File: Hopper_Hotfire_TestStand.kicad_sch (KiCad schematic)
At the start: 28 parts

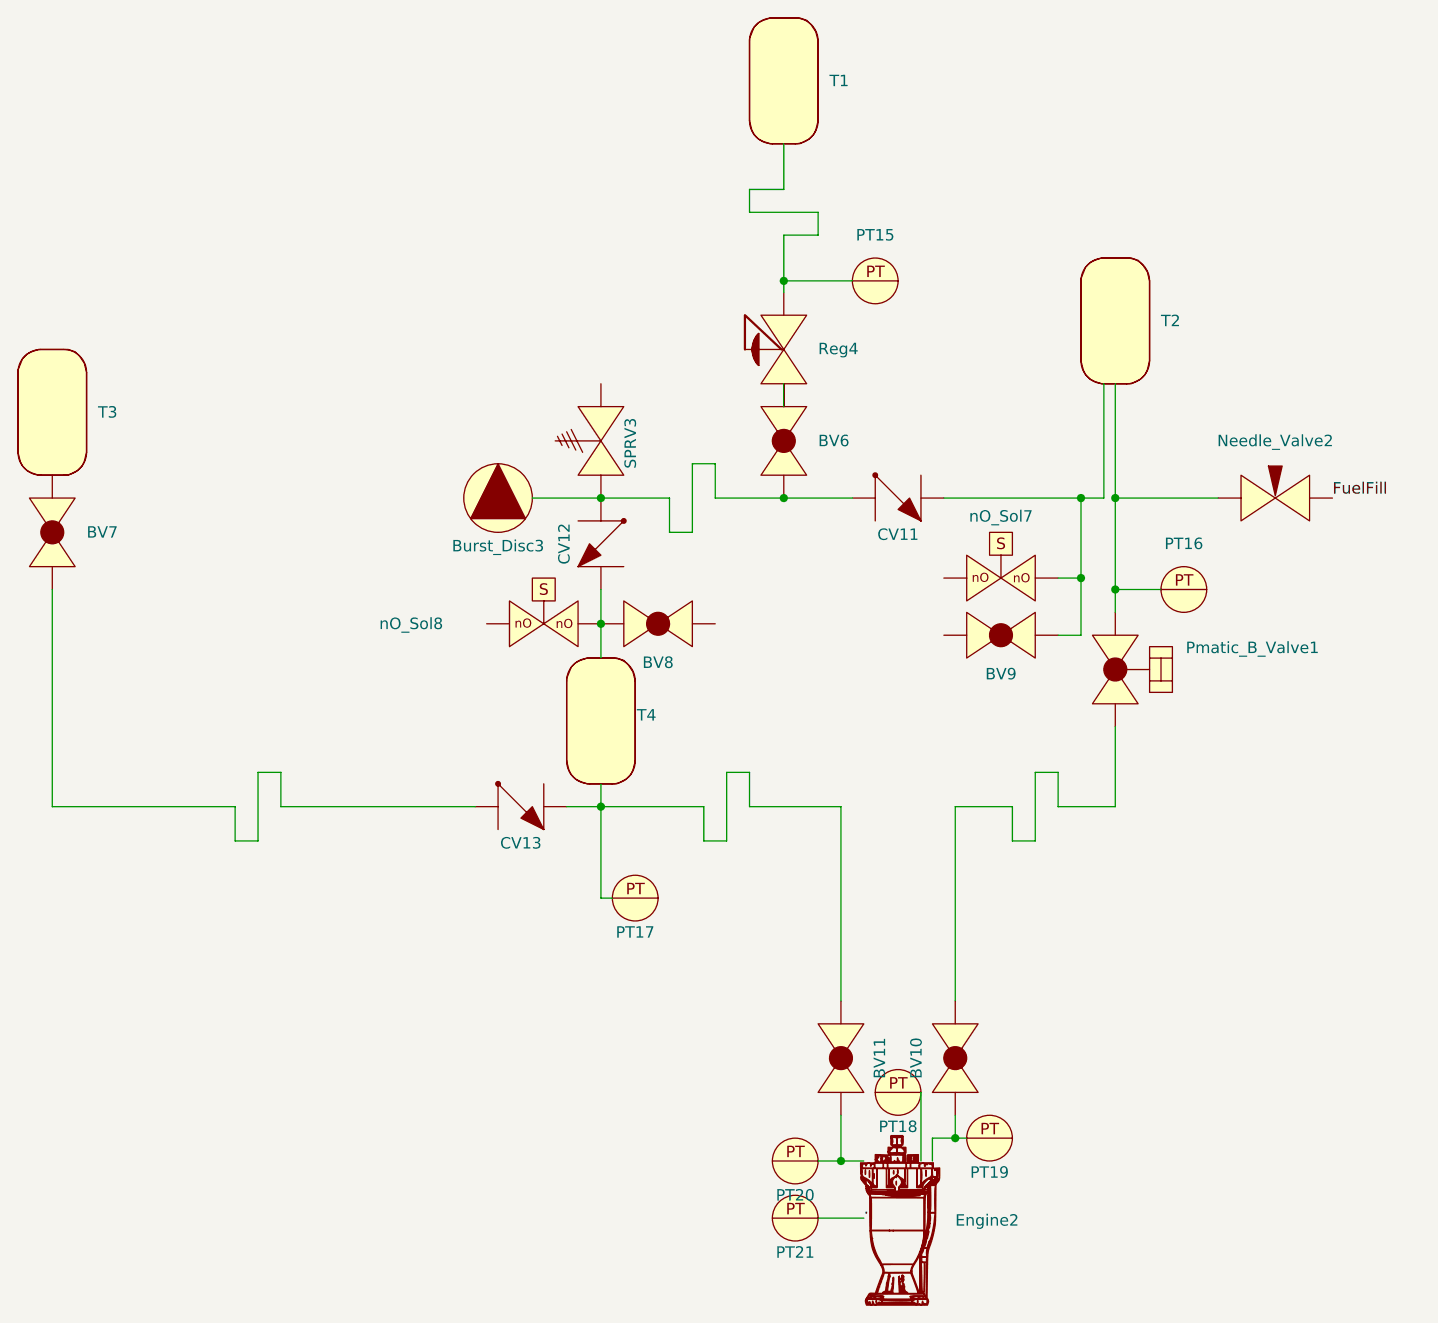
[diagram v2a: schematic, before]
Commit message: replaced servo with solenoid
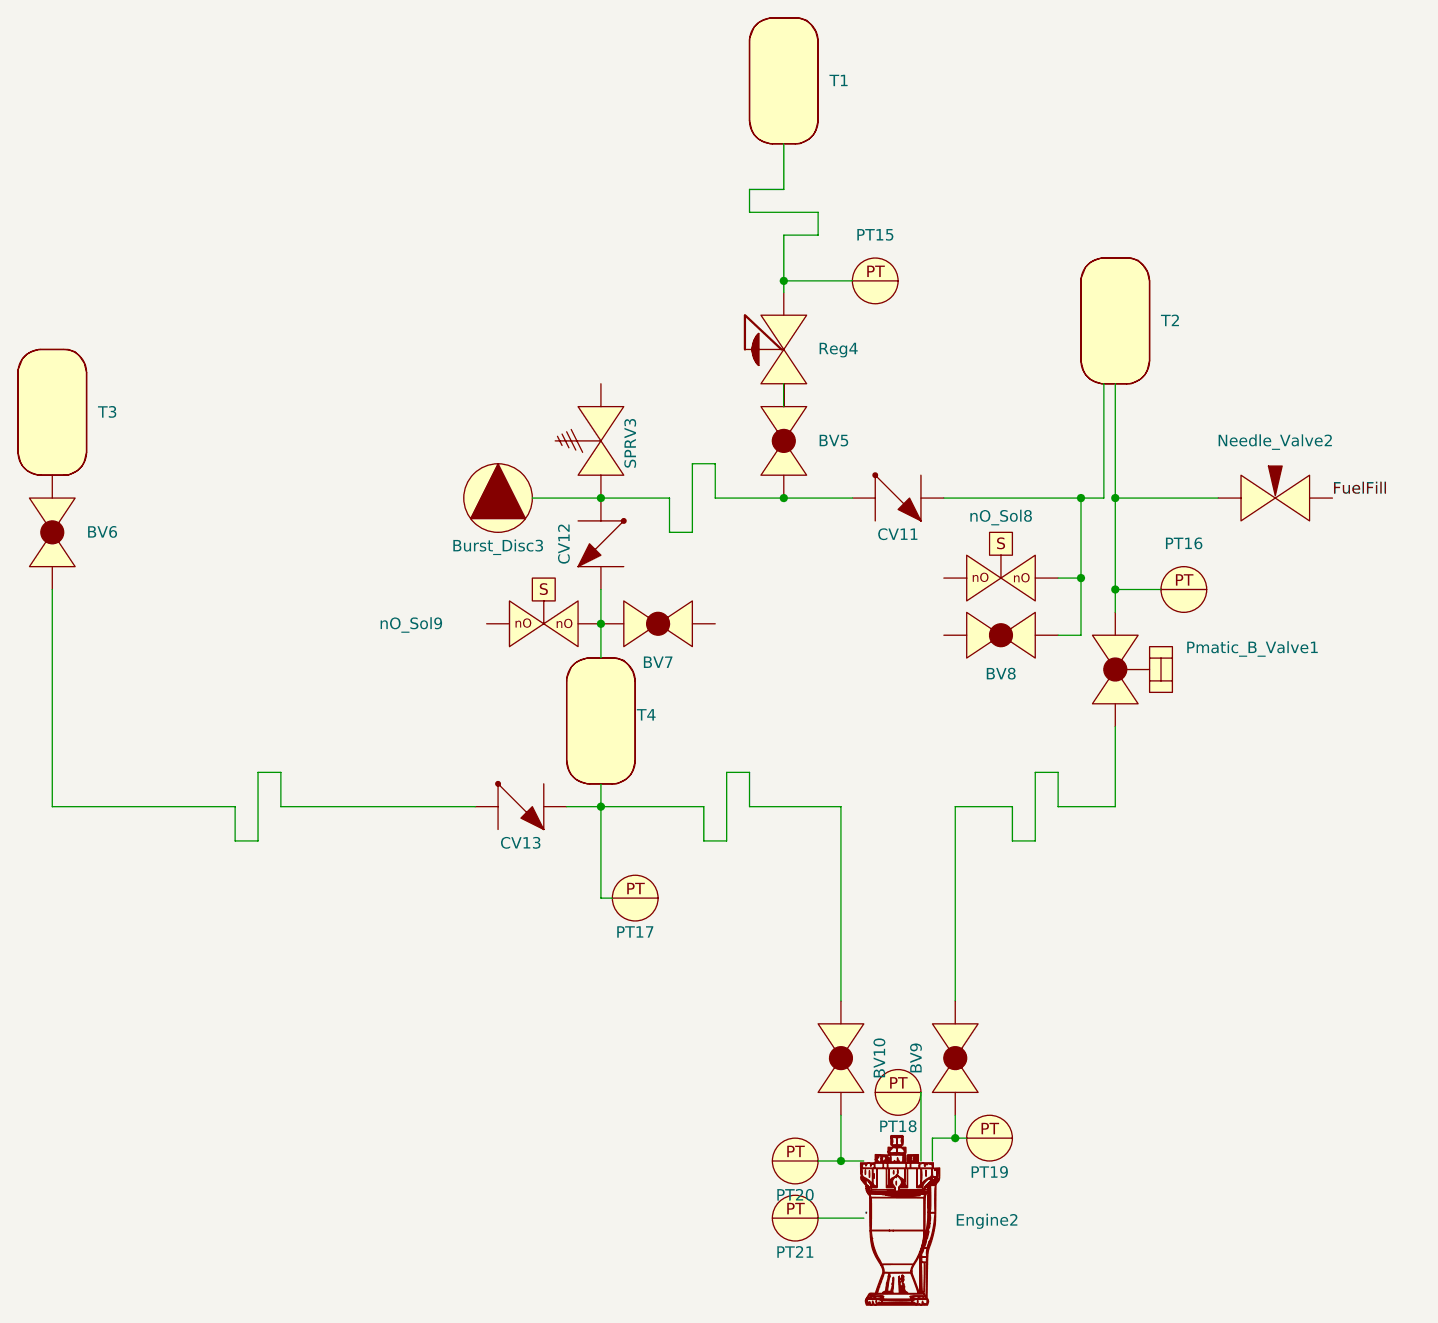
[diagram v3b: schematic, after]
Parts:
- renumbered BV11 to BV10, BV6 to BV5, BV7 to BV6, BV8 to BV7, BV9 to BV8, BV10 to BV9, nO_Sol7 to nO_Sol8, nO_Sol8 to nO_Sol9
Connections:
- net at CV13.: now also BV10., PT17., T4.; no longer BV6.
- net at BV8.: now also CV11., nO_Sol8.
- net at PT19.: now also BV9., Engine2.
- net at Pmatic_B_Valve1.: now also BV9.
- net at PT15.: now also Reg4., T1.
- new net: BV6., CV13.
- new net: BV10., Engine2., PT20.
- new net: BV5., Burst_Disc3., CV11., CV12., SPRV3.
- new net: Needle_Valve2., PT16., Pmatic_B_Valve1., T2.
- now unconnected: Burst_Disc3., Engine2., Engine2., PT16., PT17., PT20., SPRV3., T1., T2., nO_Sol8.
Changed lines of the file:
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@@
 		(dnp no)
 		(fields_autoplaced yes)
-		(property "Reference" "BV7"
+		(property "Reference" "BV6"
 			(at 53.34 73.6599 90)
 			(effects
@@
 			(project "P_IDs"
 				(path "/045f1f05-3134-4b6d-91b6-463031104f1e/12264f82-10ad-4f8b-aee0-7883d457c15c"
-					(reference "BV7")
+					(reference "BV6")
 					(unit 1)
 				)
@@
 		(on_board yes)
 		(dnp no)
-		(property "Reference" "BV9"
+		(property "Reference" "BV8"
 			(at 154.94 89.408 0)
 			(effects
@@
 			(project "P_IDs"
 				(path "/045f1f05-3134-4b6d-91b6-463031104f1e/12264f82-10ad-4f8b-aee0-7883d457c15c"
-					(reference "BV9")
+					(reference "BV8")
 					(unit 1)
 				)
@@
 		(on_board yes)
 		(dnp no)
-		(property "Reference" "BV11"
+		(property "Reference" "BV10"
 			(at 141.478 132.08 0)
 			(effects
@@
 			(project "P_IDs"
 				(path "/045f1f05-3134-4b6d-91b6-463031104f1e/12264f82-10ad-4f8b-aee0-7883d457c15c"
-					(reference "BV11")
+					(reference "BV10")
 					(unit 1)
 				)
@@
 		(on_board yes)
 		(dnp no)
-		(property "Reference" "nO_Sol7"
+		(property "Reference" "nO_Sol8"
 			(at 154.94 71.882 0)
 			(effects
@@
 			(project "P_IDs"
 				(path "/045f1f05-3134-4b6d-91b6-463031104f1e/12264f82-10ad-4f8b-aee0-7883d457c15c"
-					(reference "nO_Sol7")
+					(reference "nO_Sol8")
 					(unit 1)
 				)
@@
 		(dnp no)
 		(fields_autoplaced yes)
-		(property "Reference" "BV6"
+		(property "Reference" "BV5"
 			(at 134.62 63.4999 90)
 			(effects
@@
 			(project "P_IDs"
 				(path "/045f1f05-3134-4b6d-91b6-463031104f1e/12264f82-10ad-4f8b-aee0-7883d457c15c"
-					(reference "BV6")
+					(reference "BV5")
 					(unit 1)
 				)
@@
 		(on_board yes)
 		(dnp no)
-		(property "Reference" "BV8"
+		(property "Reference" "BV7"
 			(at 116.84 88.138 0)
 			(effects
@@
 			(project "P_IDs"
 				(path "/045f1f05-3134-4b6d-91b6-463031104f1e/12264f82-10ad-4f8b-aee0-7883d457c15c"
-					(reference "BV8")
+					(reference "BV7")
 					(unit 1)
 				)
@@
 		(on_board yes)
 		(dnp no)
-		(property "Reference" "nO_Sol8"
+		(property "Reference" "nO_Sol9"
 			(at 89.408 83.82 0)
 			(effects
@@
 			(project "P_IDs"
 				(path "/045f1f05-3134-4b6d-91b6-463031104f1e/12264f82-10ad-4f8b-aee0-7883d457c15c"
-					(reference "nO_Sol8")
+					(reference "nO_Sol9")
 					(unit 1)
 				)
@@
 		(on_board yes)
 		(dnp no)
-		(property "Reference" "BV10"
+		(property "Reference" "BV9"
 			(at 145.542 132.08 0)
 			(effects
@@
 			(project "P_IDs"
 				(path "/045f1f05-3134-4b6d-91b6-463031104f1e/12264f82-10ad-4f8b-aee0-7883d457c15c"
-					(reference "BV10")
-					(unit 1)
-				)
+					(reference "BV9")
+					(unit 1)
+				)

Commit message: rebase
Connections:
- net at CV13.: now also BV10., PT17., T4.; no longer BV6.
- net at BV8.: now also CV11., nO_Sol8.
- net at PT19.: now also BV9., Engine2.
- net at Pmatic_B_Valve1.: now also BV9.
- net at PT15.: now also Reg4., T1.
- new net: BV6., CV13.
- new net: BV10., Engine2., PT20.
- new net: BV5., Burst_Disc3., CV11., CV12., SPRV3.
- new net: Needle_Valve2., PT16., Pmatic_B_Valve1., T2.
- now unconnected: Burst_Disc3., Engine2., Engine2., PT16., PT17., PT20., SPRV3., T1., T2., nO_Sol8.
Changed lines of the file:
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@@
 	(label "."
 		(at 139.7 149.86 0)
+		(fields_autoplaced yes)
 		(effects
 			(font
@@
 	(label "FuelFill"
 		(at 191.77 69.85 0)
+		(fields_autoplaced yes)
 		(effects
 			(font
